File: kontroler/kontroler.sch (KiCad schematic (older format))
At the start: 44 parts, among them IC1 ATTINY841-SSU, P1 CONN_01X01, P2 CONN_01X01, P3 CONN_01X01, P4 CONN_01X01, P5 CONN_01X06, P6 CONN_01X06, P7 CONN_01X06, Q1 Q_PMOS_GDSD, Q2 Q_NPN_BEC, Q3 IRF8721PBF-1, Q4 Q_NMOS_GDSD, Q5 Q_NMOS_GDSD, Q6 Q_NMOS_GDSD, SW1 SW_PUSH, SW2 SW_PUSH, SW3 SW_PUSH, SW4 SW_PUSH, U1 LD1117S50CTR

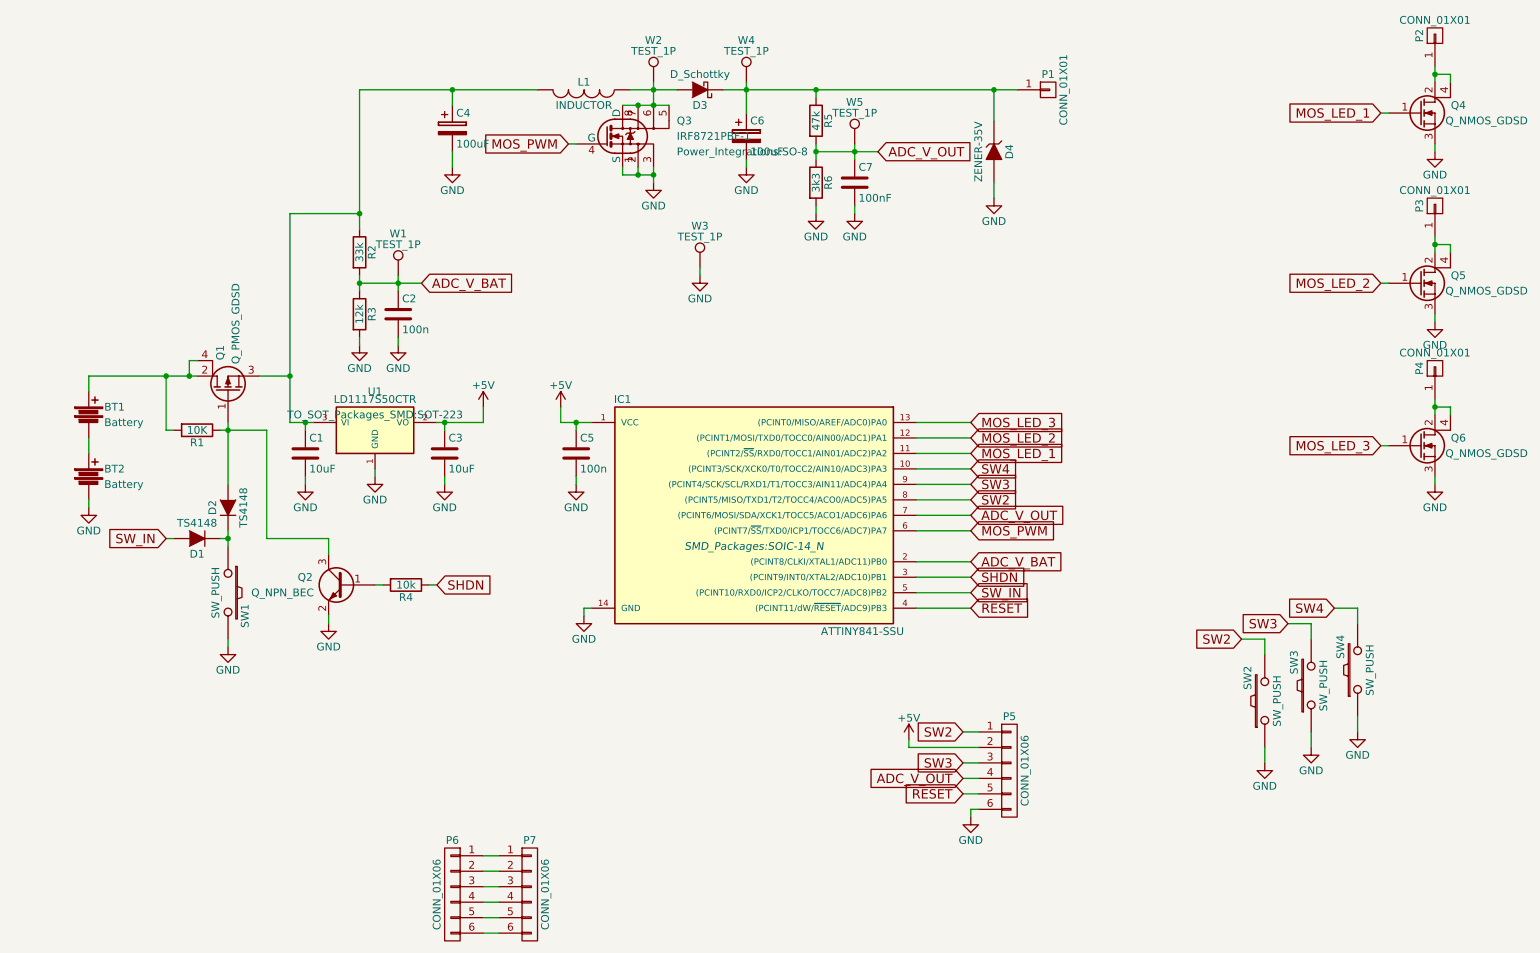
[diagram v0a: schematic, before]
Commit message: Fixed wrong p-mos orientation
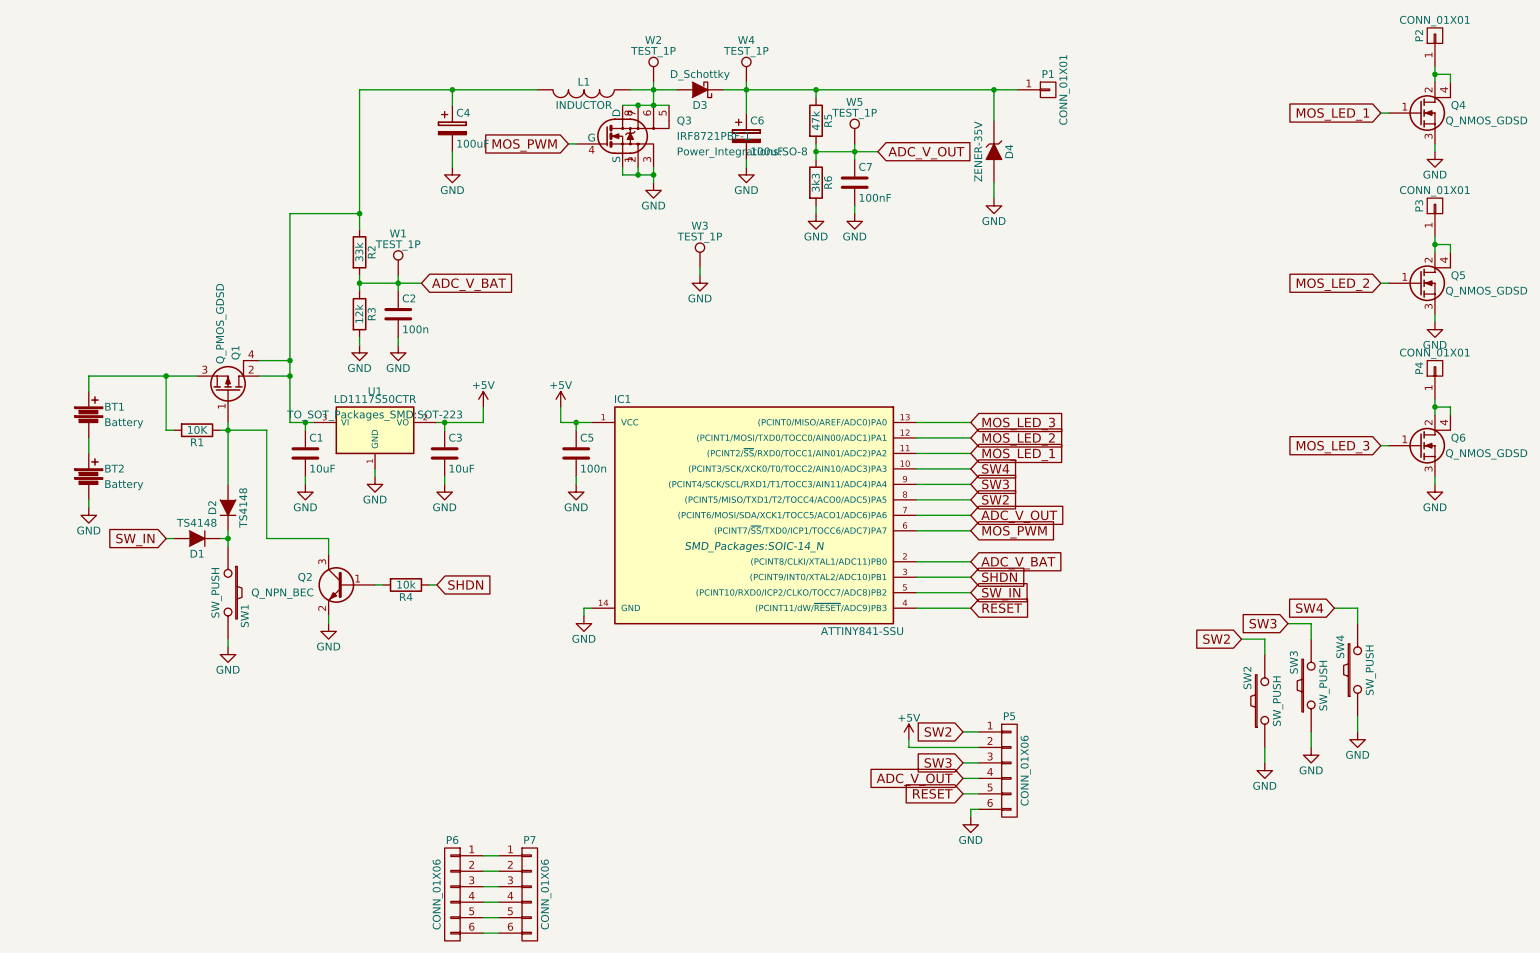
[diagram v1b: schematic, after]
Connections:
- net at BT1.1, R1.2: now also Q1.3 (S); no longer Q1.2 (D), Q1.4 (D)
- net at C1.1, C4.1, L1.2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: now also Q1.2 (D), Q1.4 (D); no longer Q1.3 (S)

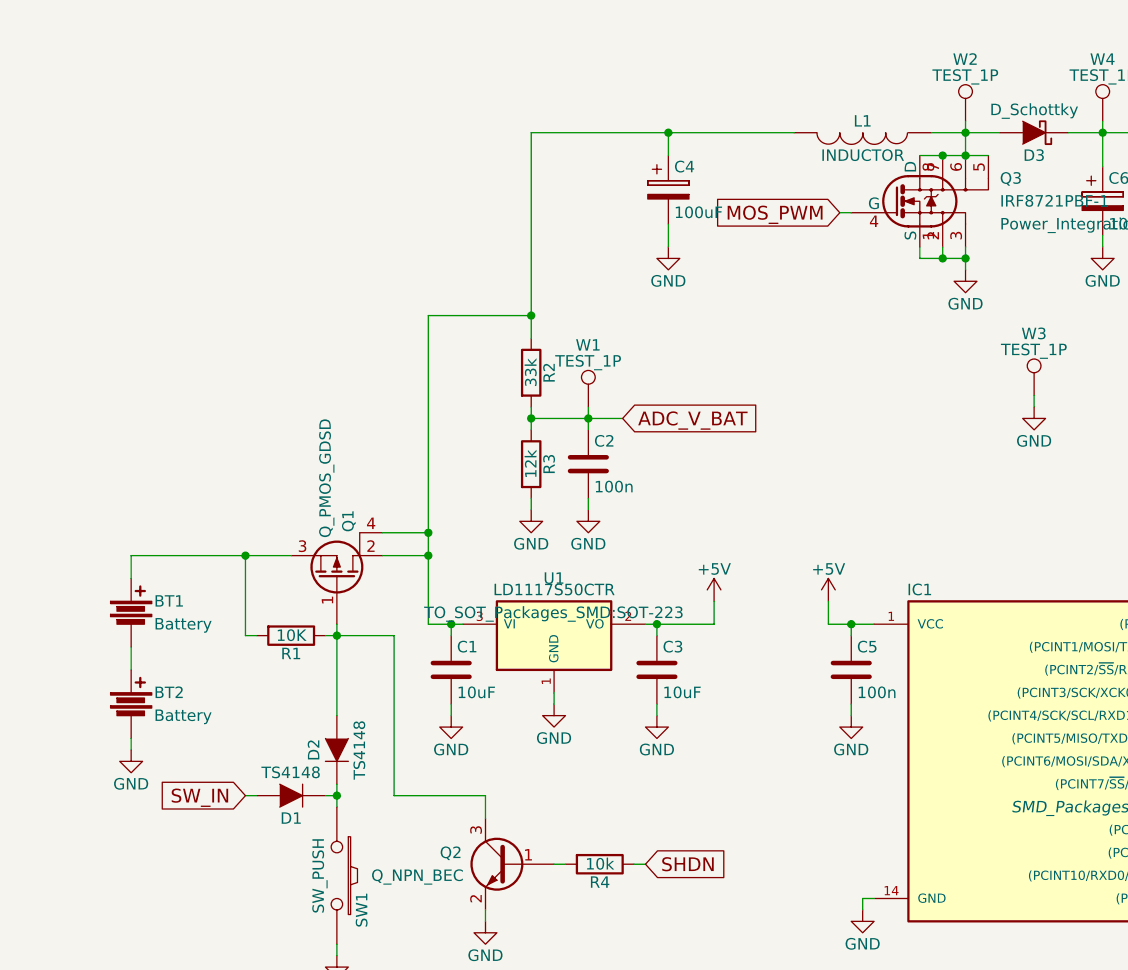
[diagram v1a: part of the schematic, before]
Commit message: Added polarity protection mosfet.
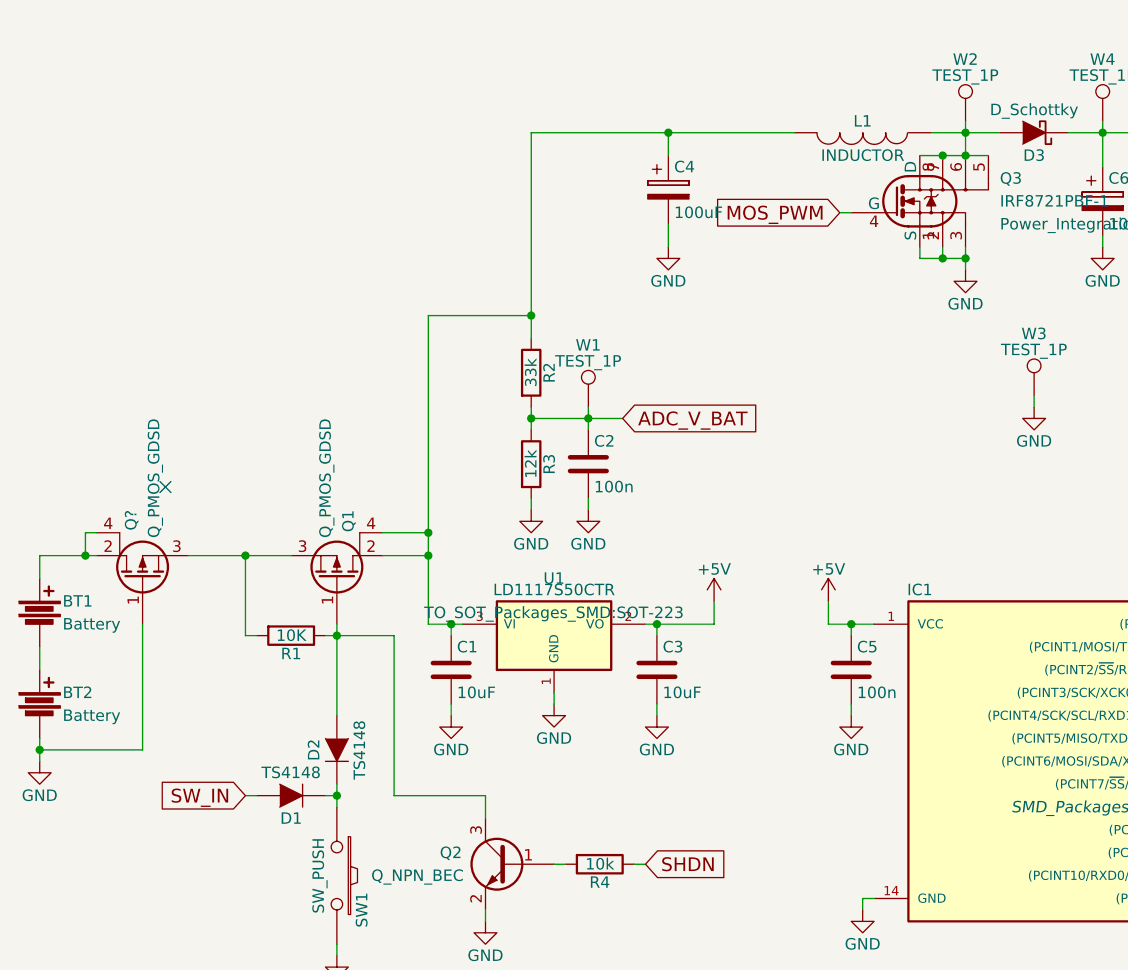
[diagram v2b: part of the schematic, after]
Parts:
- added Q?: Q_PMOS_GDSD, TO_SOT_Packages_SMD:SOT-223, symbol Q_PMOS_GDSD
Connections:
- net GND: now also Q?.1 (G)
- net at Q1.3 (S), R1.2: now also Q?.3 (S); no longer BT1.1
- new net: BT1.1, Q?.2 (D), Q?.4 (D)
- no-connect marks 0 -> 1
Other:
- moved on the sheet: BT1, BT2
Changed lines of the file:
@@
 L Battery BT1
 U 1 1 57B88D80
-P 1800 3200
-F 0 "BT1" H 1900 3250 50  0000 L CNN
-F 1 "Battery" H 1900 3150 50  0000 L CNN
-F 2 "halfbattery:HALFBATTERY" V 1800 3240 50  0001 C CNN
-F 3 "" V 1800 3240 50  0000 C CNN
-	1    1800 3200
+P 1400 3200
+F 0 "BT1" H 1500 3250 50  0000 L CNN
+F 1 "Battery" H 1500 3150 50  0000 L CNN
+F 2 "halfbattery:HALFBATTERY" V 1400 3240 50  0001 C CNN
+F 3 "" V 1400 3240 50  0000 C CNN
+	1    1400 3200
 	1    0    0    -1
 $EndComp
@@
 L Battery BT2
 U 1 1 57B88E2F
-P 1800 3600
-F 0 "BT2" H 1900 3650 50  0000 L CNN
-F 1 "Battery" H 1900 3550 50  0000 L CNN
-F 2 "halfbattery:HALFBATTERY" V 1800 3640 50  0001 C CNN
-F 3 "" V 1800 3640 50  0000 C CNN
-	1    1800 3600
+P 1400 3600
+F 0 "BT2" H 1500 3650 50  0000 L CNN
+F 1 "Battery" H 1500 3550 50  0000 L CNN
+F 2 "halfbattery:HALFBATTERY" V 1400 3640 50  0001 C CNN
+F 3 "" V 1400 3640 50  0000 C CNN
+	1    1400 3600
 	1    0    0    -1
 $EndComp
@@
 L GND #PWR01
 U 1 1 57B893DD
-P 1800 3800
-F 0 "#PWR01" H 1800 3550 50  0001 C CNN
-F 1 "GND" H 1800 3650 50  0000 C CNN
-F 2 "" H 1800 3800 50  0000 C CNN
-F 3 "" H 1800 3800 50  0000 C CNN
-	1    1800 3800
+P 1400 3850
+F 0 "#PWR01" H 1400 3600 50  0001 C CNN
+F 1 "GND" H 1400 3700 50  0000 C CNN
+F 2 "" H 1400 3850 50  0000 C CNN
+F 3 "" H 1400 3850 50  0000 C CNN
+	1    1400 3850
 	1    0    0    -1
 $EndComp
@@
 	1    0    0    -1
 $EndComp
+$Comp
+L Q_PMOS_GDSD Q?
+U 1 1 580F6BA0
+P 1850 3050
+F 0 "Q?" H 2150 3100 50  0000 R CNN
+F 1 "Q_PMOS_GDSD" H 2550 3000 50  0000 R CNN
+F 2 "TO_SOT_Packages_SMD:SOT-223" H 2050 3150 50  0001 C CNN
+F 3 "" H 1850 3050 50  0000 C CNN
+	1    1850 3050
+	0    -1   -1   0
+$EndComp
+NoConn ~ 1950 2650
 Connection ~ 3100 2850
 Wire Wire Line
 	2900 2850 3100 2850
 Wire Wire Line
-	2900 2950 3100 2950
+	3100 2950 2900 2950
 Wire Wire Line
 	4450 6550 4350 6550
@@
 Connection ~ 5450 1100
 Wire Wire Line
-	5450 1200 5450 1050
+	5450 1050 5450 1200
 Wire Wire Line
 	5300 1100 5600 1100
 Wire Wire Line
-	2950 4000 2950 3300
-Wire Wire Line
-	3350 4000 2950 4000
+	2950 3300 2950 4000
+Wire Wire Line
+	2950 4000 3350 4000
 Wire Wire Line
 	2650 4000 2700 4000
@@
 	5050 4450 5000 4450
 Wire Wire Line
-	1800 3800 1800 3750
+	1400 3850 1400 3750
 Connection ~ 4100 3250
 Wire Wire Line
@@
 Connection ~ 2300 2950
 Wire Wire Line
-	1800 3050 1800 2950
+	1400 3050 1400 2950
 Wire Wire Line
 	2700 3250 2700 3650
@@
 	2650 3300 2950 3300
 Wire Wire Line
-	1800 2950 2500 2950
+	2050 2950 2500 2950
 Wire Wire Line
 	2300 3300 2300 2950
@@
 	2350 3300 2300 3300
 Wire Wire Line
-	1800 3350 1800 3450
+	1400 3350 1400 3450
+Wire Wire Line
+	1400 2950 1650 2950
+Wire Wire Line
+	1650 2850 1600 2850
+Wire Wire Line
+	1600 2850 1600 2950
+Connection ~ 1600 2950
+Wire Wire Line
+	1850 3250 1850 3800
+Wire Wire Line
+	1850 3800 1400 3800
+Connection ~ 1400 3800
 $EndSCHEMATC
